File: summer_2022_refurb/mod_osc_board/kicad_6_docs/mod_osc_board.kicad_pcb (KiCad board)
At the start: 2 copper layers, 123.2 x 76.2 mm, 77 parts, among them J1 ext_port, J2 ribbon_board_port, J3 adsr_board_port, J4 vco_board_port, J5 vcf_board_port, J6 power_entry, SW101 SW_SPDT_MSM, SW201 alpha_SR2612F-0112, U201 SSI2130, U202 TL072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

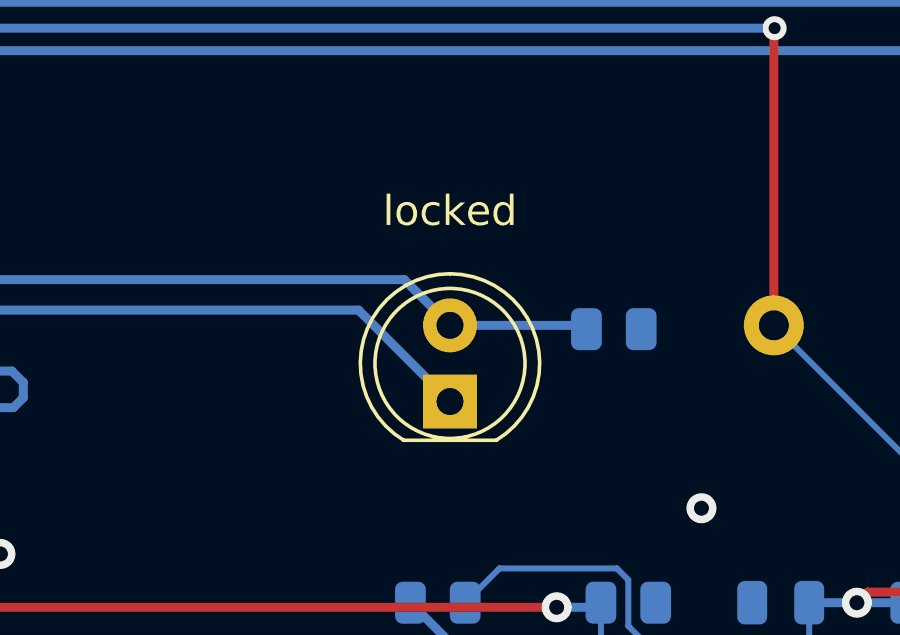
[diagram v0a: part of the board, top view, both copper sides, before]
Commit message: Change directory structure, minor schem and pcb tweaks
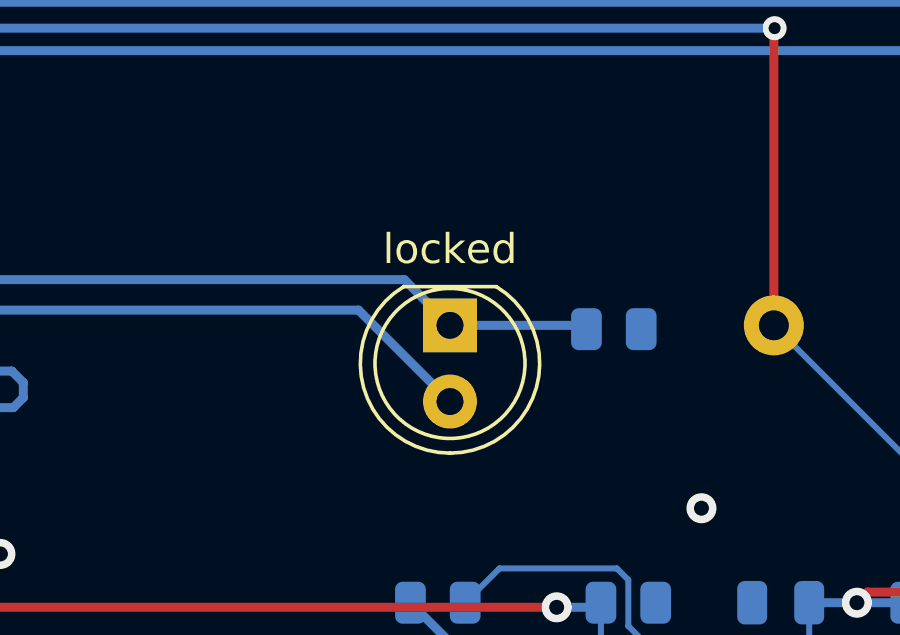
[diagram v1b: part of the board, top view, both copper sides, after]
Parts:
- moved locked 2.54 mm to (100.3, 53.3), turned to -90 degrees
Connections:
- R401 pad 2: Net-(D401-Pad2) -> Net-(R401-Pad2)
- U301 pad 6: Net-(D401-Pad2) -> Net-(R401-Pad2)
- U301 pad 7: Net-(D401-Pad1) -> Net-(U301-Pad7)
- locked pad 1: Net-(D401-Pad1) -> Net-(R401-Pad2)
- locked pad 2: Net-(D401-Pad2) -> Net-(U301-Pad7)
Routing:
- net Net-(R401-Pad2): track 0.00 -> 40.3 mm
- net Net-(D401-Pad2): track 40.3 -> 0.00 mm
- net Net-(U301-Pad7): track 0.00 -> 32.8 mm
- net Net-(D401-Pad1): track 32.8 -> 0.00 mm
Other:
- board text added: "Mod Osc board rev 0 2022-06-16"
- board text removed: "Mod Osc board rev 0 2022-06-14"
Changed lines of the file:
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@@
   (title_block
     (title "Josh Ox Ribbon Synth Mod Osc board")
-    (date "2022-06-14")
+    (date "2022-06-16")
     (rev "0")
     (comment 2 "creativecommons.org/licences/by/4.0")
@@
   (net 11 "-5V")
   (net 12 "Net-(D201-Pad2)")
-  (net 13 "Net-(D401-Pad1)")
-  (net 14 "Net-(D401-Pad2)")
+  (net 13 "Net-(R401-Pad2)")
+  (net 14 "Net-(U301-Pad7)")
   (net 15 "/VCO_core/V_PER_OCT_IN_1")
   (net 16 "/VCO_core/V_PER_OCT_IN_2")
@@
     )
   )
-  (footprint "LED_THT:LED_D5.0mm" (layer "F.Cu")
-    (at 100.33 55.88 90)
+  (footprint "LED_THT:LED_D5.0mm" locked (layer "F.Cu")
+    (at 100.33 53.34 -90)
     (descr "LED, diameter 5.0mm, 2 pins, http://cdn-reichelt.de/documents/datenblatt/A500/LL-504BC2E-009.pdf")
     (tags "LED diameter 5.0mm 2 pins")
@@
     (property "Sheetname" "led_driver")
     (attr through_hole)
-    (fp_text reference locked "D401" (at 6.35 0.000462 180) (layer "F.SilkS")
+    (fp_text reference locked "D401" (at -2.54 0) (layer "F.SilkS")
       (effects (font (size 1 1) (thickness 0.15)))
     )
@@
     (fp_arc (start -1.23 -1.469694) (mid 4.17 0.000016) (end -1.230016 1.469666) (layer "F.Fab") (width 0.1))
     (fp_circle (center 1.27 0) (end 3.77 0) (layer "F.Fab") (width 0.1) (fill none))
-    (pad "1" thru_hole rect (at 0 0 90) (size 1.8 1.8) (drill 0.9) (layers *.Cu *.Mask)
-      (net 13 "Net-(D401-Pad1)") (pinfunction "KA") (pintype "input"))
-    (pad "2" thru_hole circle (at 2.54 0 90) (size 1.8 1.8) (drill 0.9) (layers *.Cu *.Mask)
-      (net 14 "Net-(D401-Pad2)") (pinfunction "AK") (pintype "input"))
+    (pad "1" thru_hole rect locked (at 0 0 270) (size 1.8 1.8) (drill 0.9) (layers *.Cu *.Mask)
+      (net 13 "Net-(R401-Pad2)") (pinfunction "KA") (pintype "input"))
+    (pad "2" thru_hole circle locked (at 2.54 0 270) (size 1.8 1.8) (drill 0.9) (layers *.Cu *.Mask)
+      (net 14 "Net-(U301-Pad7)") (pinfunction "AK") (pintype "input"))
     (model "${KICAD6_3DMODEL_DIR}/LED_THT.3dshapes/LED_D5.0mm.wrl"
       (offset (xyz 0 0 0))
@@
       (net 8 "/MOD_OSC_OUT") (pinfunction "+") (pintype "input"))
     (pad "6" smd roundrect (at 3.5 -0.635 180) (size 1.9 0.6) (layers "B.Cu" "B.Paste" "B.Mask") (roundrect_rratio 0.25)
-      (net 14 "Net-(D401-Pad2)") (pinfunction "-") (pintype "input"))
+      (net 13 "Net-(R401-Pad2)") (pinfunction "-") (pintype "input"))
     (pad "7" smd roundrect (at 3.5 0.635 180) (size 1.9 0.6) (layers "B.Cu" "B.Paste" "B.Mask") (roundrect_rratio 0.25)
-      (net 13 "Net-(D401-Pad1)") (pintype "output"))
+      (net 14 "Net-(U301-Pad7)") (pintype "output"))
     (pad "8" smd roundrect (at 3.5 1.905 180) (size 1.9 0.6) (layers "B.Cu" "B.Paste" "B.Mask") (roundrect_rratio 0.25)
       (net 9 "+15V") (pinfunction "V+") (pintype "power_in"))
@@
     (property "Sheetfile" "power_supply.kicad_sch")
     (property "Sheetname" "power_supply")
-    (attr through_hole)
+    (property "exclude_from_bom" "")
+    (attr through_hole exclude_from_bom)
     (fp_text reference "TP506" (at 0 2.5) (layer "B.SilkS")
       (effects (font (size 1 1) (thickness 0.15)) (justify mirror))
@@
     (property "Sheetfile" "power_supply.kicad_sch")
     (property "Sheetname" "power_supply")
-    (attr through_hole)
+    (property "exclude_from_bom" "")
+    (attr through_hole exclude_from_bom)
     (fp_text reference "TP504" (at 0 2.5) (layer "B.SilkS")
       (effects (font (size 1 1) (thickness 0.15)) (justify mirror))
@@
     (property "Sheetfile" "power_supply.kicad_sch")
     (property "Sheetname" "power_supply")
-    (attr through_hole)
+    (property "exclude_from_bom" "")
+    (attr through_hole exclude_from_bom)
     (fp_text reference "TP505" (at 0 2.5) (layer "B.SilkS")
       (effects (font (size 1 1) (thickness 0.15)) (justify mirror))
@@
     (property "Sheetfile" "mod_osc_board.kicad_sch")
     (property "Sheetname" "")
-    (attr through_hole)
+    (property "exclude_from_bom" "")
+    (attr through_hole exclude_from_bom)
     (fp_text reference "TP102" (at 0 2.5) (layer "B.SilkS")
       (effects (font (size 1 1) (thickness 0.15)) (justify mirror))
@@
     (property "Sheetfile" "power_supply.kicad_sch")
     (property "Sheetname" "power_supply")
-    (attr through_hole)
+    (property "exclude_from_bom" "")
+    (attr through_hole exclude_from_bom)
     (fp_text reference "TP503" (at 3.3 -2.4) (layer "B.SilkS")
       (effects (font (size 1 1) (thickness 0.15)) (justify mirror))
@@
       (net 3 "GND") (pintype "passive"))
     (pad "2" smd roundrect (at 0.9125 0 180) (size 1.025 1.4) (layers "B.Cu" "B.Paste" "B.Mask") (roundrect_rratio 0.243902)
-      (net 14 "Net-(D401-Pad2)") (pintype "passive"))
+      (net 13 "Net-(R401-Pad2)") (pintype "passive"))
     (model "${KICAD6_3DMODEL_DIR}/Resistor_SMD.3dshapes/R_0805_2012Metric.wrl"
       (offset (xyz 0 0 0))
@@
     (property "Sheetfile" "power_supply.kicad_sch")
     (property "Sheetname" "power_supply")
-    (attr through_hole)
+    (property "exclude_from_bom" "")
+    (attr through_hole exclude_from_bom)
     (fp_text reference "TP502" (at 0 2.5) (layer "B.SilkS")
       (effects (font (size 1 1) (thickness 0.15)) (justify mirror))
@@
     (property "Sheetfile" "mod_osc_board.kicad_sch")
     (property "Sheetname" "")
-    (attr through_hole)
+    (property "exclude_from_bom" "")
+    (attr through_hole exclude_from_bom)
     (fp_text reference "TP101" (at 0 2.5) (layer "B.SilkS")
       (effects (font (size 1 1) (thickness 0.15)) (justify mirror))
@@
     (property "Sheetfile" "power_supply.kicad_sch")
     (property "Sheetname" "power_supply")
-    (attr through_hole)
+    (property "exclude_from_bom" "")
+    (attr through_hole exclude_from_bom)
     (fp_text reference "TP501" (at 0 2.5) (layer "B.SilkS")
       (effects (font (size 1 1) (thickness 0.15)) (justify mirror))
@@
     (effects (font (size 1 1) (thickness 0.15)) (justify right mirror))
   )
-  (gr_text "Mod Osc board\nrev 0\n2022-06-14" (at 133.35 109.22) (layer "B.SilkS")
+  (gr_text "Mod Osc board\nrev 0\n2022-06-16" (at 133.35 109.22) (layer "B.SilkS")
     (effects (font (size 1 1) (thickness 0.15)) (justify left mirror))
   )
@@
   (segment (start 113.0524 74.1456) (end 112.014 75.184) (width 0.2) (layer "B.Cu") (net 12))
   (segment (start 105.3611 77.8256) (end 107.1861 76.0006) (width 0.3) (layer "B.Cu") (net 12))
-  (segment (start 97.282 52.832) (end 100.33 55.88) (width 0.3) (layer "B.Cu") (net 13))
-  (segment (start 76.51 56.0832) (end 74.4982 56.0832) (width 0.3) (layer "B.Cu") (net 13))
-  (segment (start 74.4982 56.0832) (end 74.041 55.626) (width 0.3) (layer "B.Cu") (net 13))
-  (segment (start 74.041 55.626) (end 74.041 53.213) (width 0.3) (layer "B.Cu") (net 13))
-  (segment (start 74.422 52.832) (end 97.282 52.832) (width 0.3) (layer "B.Cu") (net 13))
-  (segment (start 74.041 53.213) (end 74.422 52.832) (width 0.3) (layer "B.Cu") (net 13))
-  (segment (start 104.7515 53.34) (end 104.8785 53.467) (width 0.3) (layer "B.Cu") (net 14))
-  (segment (start 74.4982 57.3532) (end 76.51 57.3532) (width 0.3) (layer "B.Cu") (net 14))
-  (segment (start 73.787 51.816) (end 73.025 52.578) (width 0.3) (layer "B.Cu") (net 14))
-  (segment (start 98.806 51.816) (end 73.787 51.816) (width 0.3) (layer "B.Cu") (net 14))
-  (segment (start 100.33 53.34) (end 98.806 51.816) (width 0.3) (layer "B.Cu") (net 14))
-  (segment (start 73.025 55.88) (end 74.4982 57.3532) (width 0.3) (layer "B.Cu") (net 14))
-  (segment (start 73.025 52.578) (end 73.025 55.88) (width 0.3) (layer "B.Cu") (net 14))
-  (segment (start 100.33 53.34) (end 104.7515 53.34) (width 0.3) (layer "B.Cu") (net 14))
+  (segment (start 104.7515 53.34) (end 104.8785 53.467) (width 0.3) (layer "B.Cu") (net 13))
+  (segment (start 74.4982 57.3532) (end 76.51 57.3532) (width 0.3) (layer "B.Cu") (net 13))
+  (segment (start 73.787 51.816) (end 73.025 52.578) (width 0.3) (layer "B.Cu") (net 13))
+  (segment (start 98.806 51.816) (end 73.787 51.816) (width 0.3) (layer "B.Cu") (net 13))
+  (segment (start 100.33 53.34) (end 98.806 51.816) (width 0.3) (layer "B.Cu") (net 13))
+  (segment (start 73.025 55.88) (end 74.4982 57.3532) (width 0.3) (layer "B.Cu") (net 13))
+  (segment (start 73.025 52.578) (end 73.025 55.88) (width 0.3) (layer "B.Cu") (net 13))
+  (segment (start 100.33 53.34) (end 104.7515 53.34) (width 0.3) (layer "B.Cu") (net 13))
+  (segment (start 97.282 52.832) (end 100.33 55.88) (width 0.3) (layer "B.Cu") (net 14))
+  (segment (start 76.51 56.0832) (end 74.4982 56.0832) (width 0.3) (layer "B.Cu") (net 14))
+  (segment (start 74.4982 56.0832) (end 74.041 55.626) (width 0.3) (layer "B.Cu") (net 14))
+  (segment (start 74.041 55.626) (end 74.041 53.213) (width 0.3) (layer "B.Cu") (net 14))
+  (segment (start 74.422 52.832) (end 97.282 52.832) (width 0.3) (layer "B.Cu") (net 14))
+  (segment (start 74.041 53.213) (end 74.422 52.832) (width 0.3) (layer "B.Cu") (net 14))
   (segment (start 132.99408 65.48152) (end 135.0264 63.4492) (width 0.3) (layer "B.Cu") (net 15))
   (segment (start 132.99408 73.15358) (end 132.99408 65.48152) (width 0.3) (layer "B.Cu") (net 15))

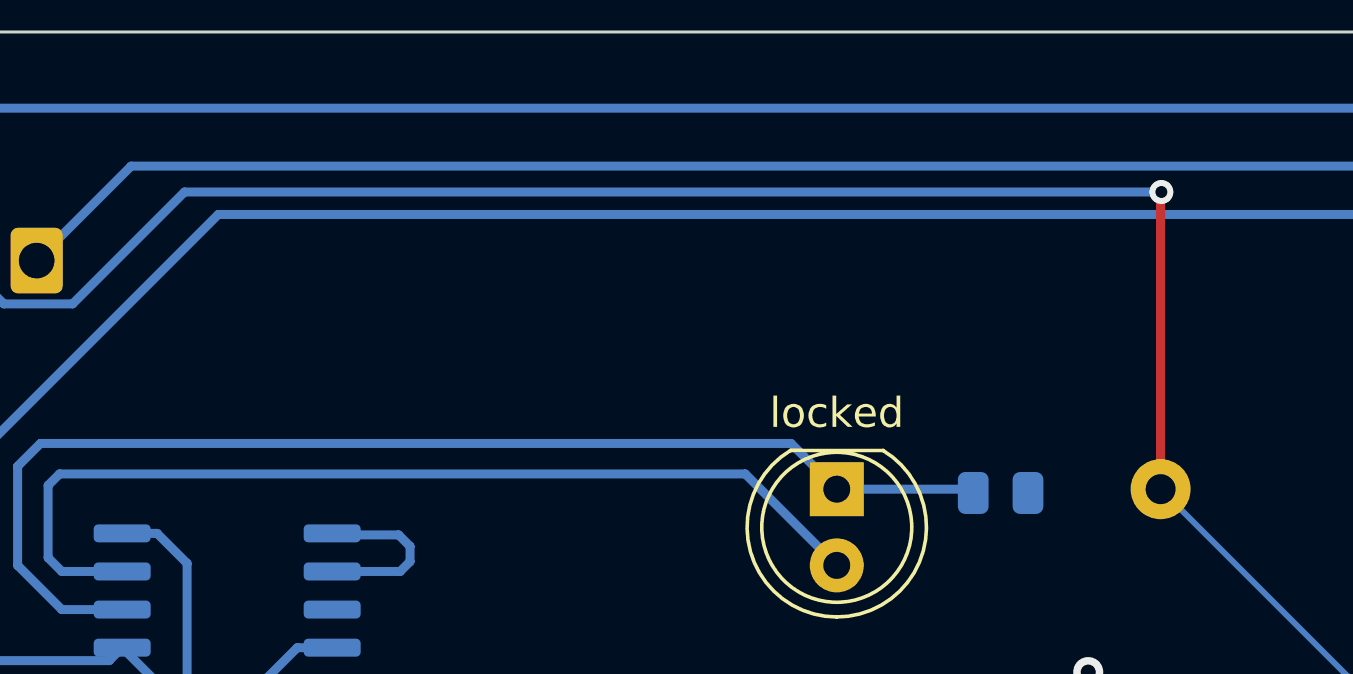
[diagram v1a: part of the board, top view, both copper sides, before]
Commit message: Add cool kibuzzard labels, minor tweaks
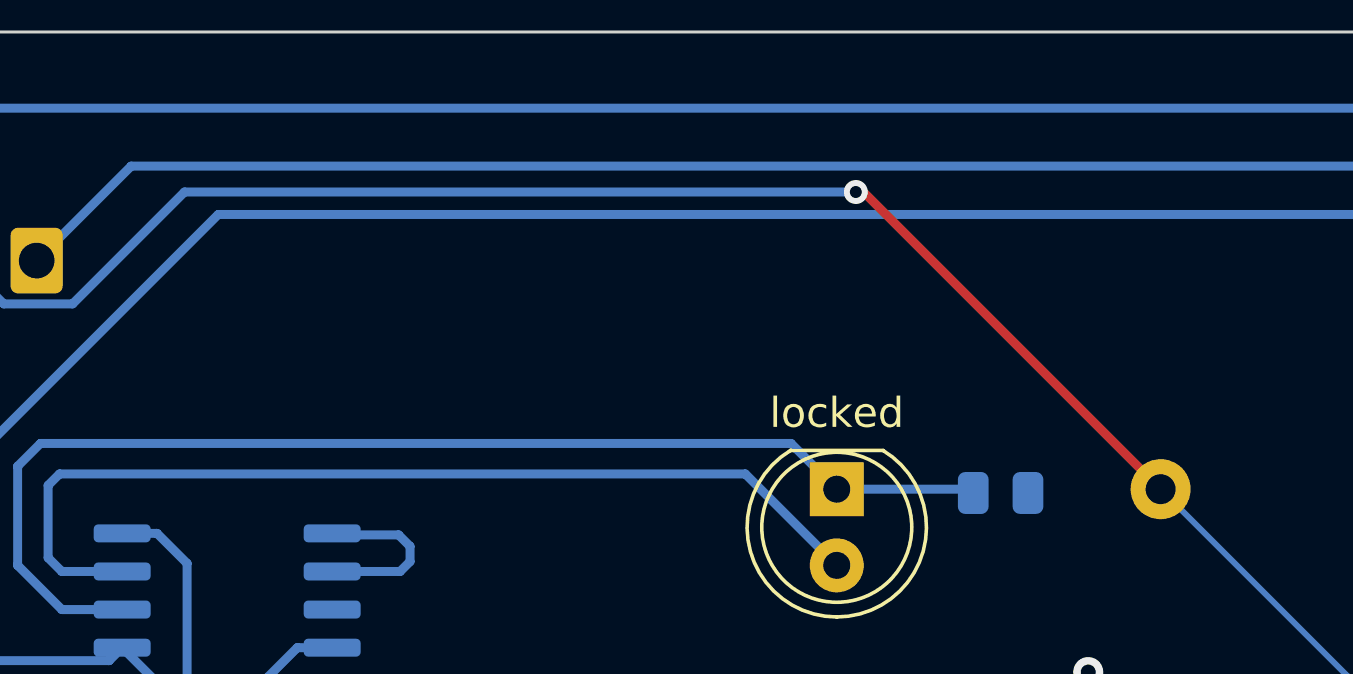
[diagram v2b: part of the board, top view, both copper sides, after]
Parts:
- added REF**: OSHW-Logo_5.7x6mm_SilkScreen, Symbol:OSHW-Logo_5.7x6mm_SilkScreen, B.Cu at (99.3, 46.5)
- added kibuzzard-62AC755C: G***, kibuzzard-62AC755C, B.Cu at (80.0, 87.0)
- added kibuzzard-62AC755C: G***, kibuzzard-62AC755C, B.Cu at (52.1, 52.1)
- added kibuzzard-62AC755C: G***, kibuzzard-62AC755C, B.Cu at (121.9, 52.1)
- added kibuzzard-62AC755C: G***, kibuzzard-62AC755C, B.Cu at (71.1, 97.8)
- added kibuzzard-62AC755C: G***, kibuzzard-62AC755C, B.Cu at (68.6, 52.1)
- added kibuzzard-62AC755C: G***, kibuzzard-62AC755C, B.Cu at (50.7, 66.0)
- added kibuzzard-62AC755C: G***, kibuzzard-62AC755C, B.Cu at (44.5, 87.0)
- added kibuzzard-62AC78CB: G***, kibuzzard-62AC78CB, B.Cu at (71.1, 111.8)
- added kibuzzard-62AC791A: G***, kibuzzard-62AC791A, B.Cu at (87.9, 92.5)
- added kibuzzard-62AC791A: G***, kibuzzard-62AC791A, B.Cu at (76.2, 97.8)
- added kibuzzard-62AC792A: G***, kibuzzard-62AC792A, B.Cu at (66.0, 83.7)
- added kibuzzard-62AC792A: G***, kibuzzard-62AC792A, B.Cu at (66.0, 97.8)
- added kibuzzard-62AC7A9F: G***, kibuzzard-62AC7A9F, B.Cu at (99.1, 40.6)
- added kibuzzard-62AC7C76: G***, kibuzzard-62AC7C76, B.Cu at (51.6, 81.3)
- added kibuzzard-62AC7C76: G***, kibuzzard-62AC7C76, B.Cu at (51.6, 63.5)
- added kibuzzard-62AC7C76: G***, kibuzzard-62AC7C76, B.Cu at (127.0, 53.0)
- added kibuzzard-62AC7CCE: G***, kibuzzard-62AC7CCE, B.Cu at (71.1, 52.6)
- added kibuzzard-62AC7CEB: G***, kibuzzard-62AC7CEB, B.Cu at (73.7, 53.8)
- added kibuzzard-62AC7D00: G***, kibuzzard-62AC7D00, B.Cu at (124.5, 52.6)
- added kibuzzard-62AC7D1D: G***, kibuzzard-62AC7D1D, B.Cu at (39.4, 82.5)
- added kibuzzard-62AC7D30: G***, kibuzzard-62AC7D30, B.Cu at (39.4, 64.8)
- added kibuzzard-62AC7D44: G***, kibuzzard-62AC7D44, B.Cu at (53.3, 40.6)
- added kibuzzard-62AC7D55: G***, kibuzzard-62AC7D55, B.Cu at (71.1, 40.6)
- added kibuzzard-62AC7D68: G***, kibuzzard-62AC7D68, B.Cu at (124.5, 40.6)
- added kibuzzard-62AC7D79: G***, kibuzzard-62AC7D79, B.Cu at (93.3, 112.4)
- added kibuzzard-62AC7D8B: G***, kibuzzard-62AC7D8B, B.Cu at (100.3, 112.4)
- added kibuzzard-62AC7DA9: G***, kibuzzard-62AC7DA9, B.Cu at (111.1, 56.5)
- added kibuzzard-62AC7DB6: G***, kibuzzard-62AC7DB6, B.Cu at (62.9, 62.2)
- added kibuzzard-62AC7DF7: G***, kibuzzard-62AC7DF7, B.Cu at (108.6, 46.4)
- added kibuzzard-62AC7EA8: G***, kibuzzard-62AC7EA8, B.Cu at (53.3, 93.3)
- added kibuzzard-62AC7EE1: G***, kibuzzard-62AC7EE1, B.Cu at (106.3, 93.3)
- added kibuzzard-62AC7EFA: G***, kibuzzard-62AC7EFA, B.Cu at (116.5, 93.3)
- added kibuzzard-62AC7F0B: G***, kibuzzard-62AC7F0B, B.Cu at (126.6, 93.3)
- added kibuzzard-62AC911A: G***, kibuzzard-62AC911A, B.Cu at (54.6, 53.1)
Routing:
- net /VCO_core/RAW_SQUARE_OUT: track 72.0 -> 66.2 mm
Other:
- board text removed: "+2V5 ref"
- board text removed: "+5V"
- board text removed: "-5V"
- board text removed: "ADSR BOARD PORT"
- board text removed: "CV I"
- board text removed: "DC POWER IN"
- board text removed: "EXT CON PORT"
- board text removed: "GND"
- board text removed: "MOD ADSR I"
- board text removed: "MOD OSC O"
- board text removed: "Mod Osc board rev 0 2022-06-16"
- board text removed: "Ox Ribbon Synth"
- board text removed: "RIBBON BOARD PORT"
- board text removed: "RIBBON I"
- board text removed: "SQUARE O"
- board text removed: "V+"
- board text removed: "V-"
- board text removed: "VCF BOARD PORT"
- board text removed: "VCO BOARD PORT"
- board text removed: "base trim"
- board text removed: "h.f. trim"
- board text removed: "mod osc"
- board text removed: "scale trim"
- board text removed: "square"
